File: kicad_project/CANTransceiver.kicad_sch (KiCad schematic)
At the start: 18 parts, among them J10 1x2, J11 1x2, J9 1x2, M1 QPC02SXGN-RC, M2 QPC02SXGN-RC, U17 MCP2515-xST, U18 TJA1051T-3, U19 TJA1051T-3

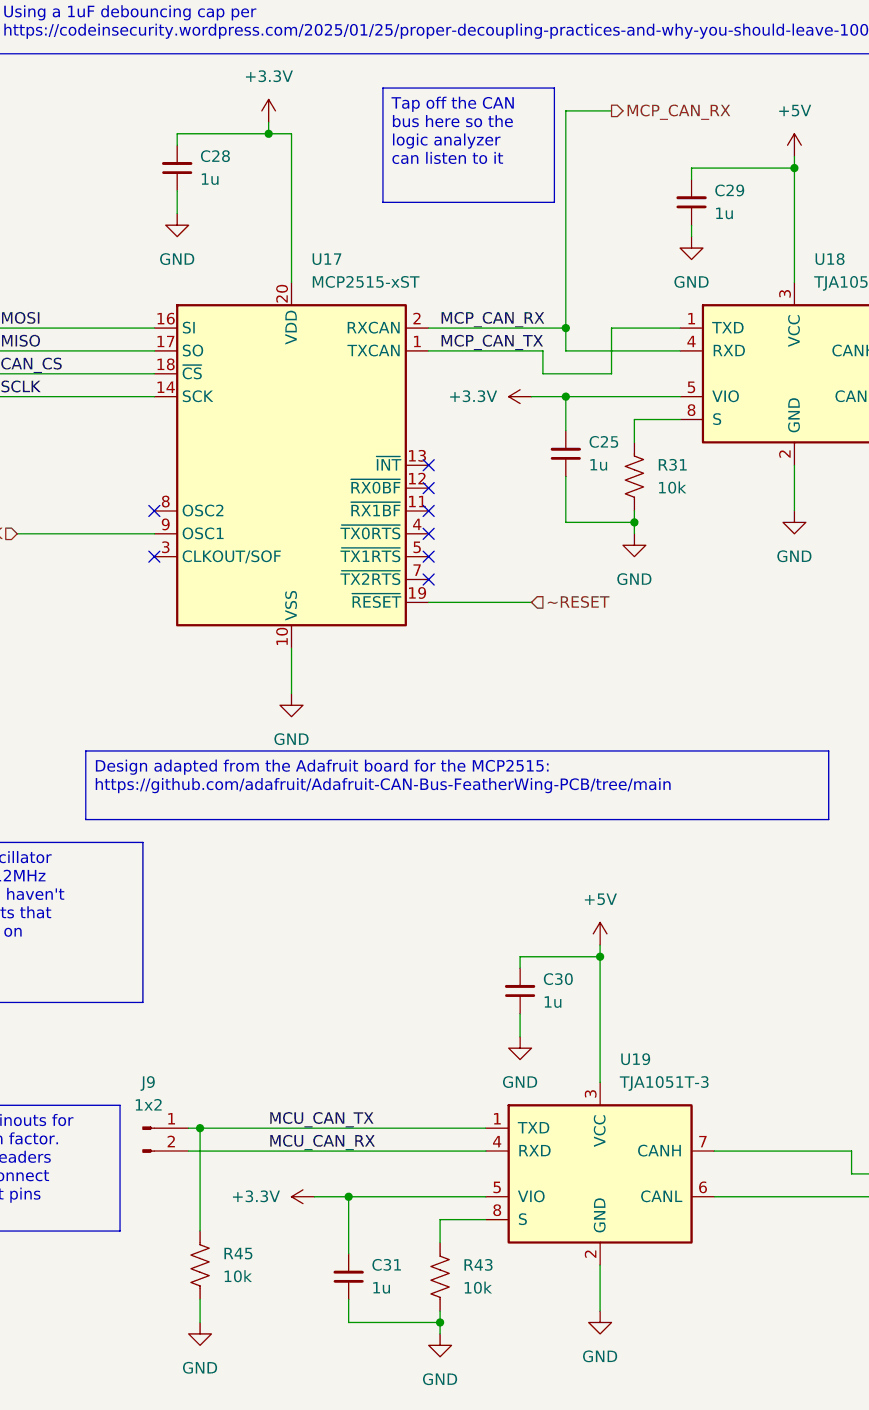
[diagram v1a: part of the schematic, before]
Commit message: Finish schematic and placement for all remaining RP2354 power passives
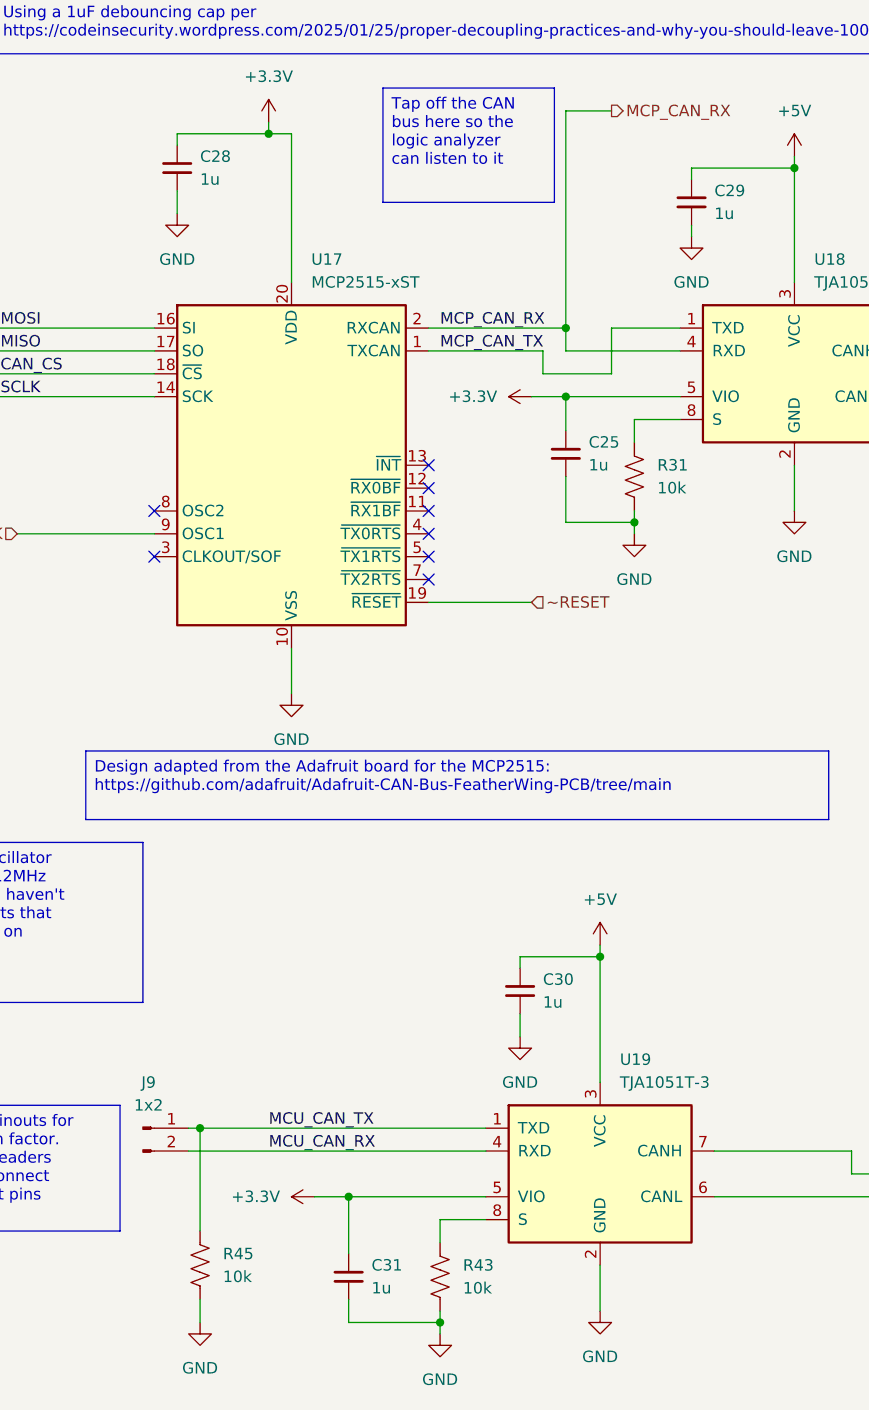
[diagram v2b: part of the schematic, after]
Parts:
- U18, U19: footprint project libraries:SOIC-8_3.9x4.9mm_P1.27mm_TJA1051T-3 -> Package_SO:SOIC-8_3.9x4.9mm_P1.27mm
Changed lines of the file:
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@@
 			)
 		)
-		(property "Footprint" "project libraries:SOIC-8_3.9x4.9mm_P1.27mm_TJA1051T-3"
+		(property "Footprint" "Package_SO:SOIC-8_3.9x4.9mm_P1.27mm"
 			(at 118.11 158.75 0)
 			(hide yes)
@@
 			)
 		)
-		(property "Footprint" "project libraries:SOIC-8_3.9x4.9mm_P1.27mm_TJA1051T-3"
+		(property "Footprint" "Package_SO:SOIC-8_3.9x4.9mm_P1.27mm"
 			(at 139.7 69.85 0)
 			(hide yes)
